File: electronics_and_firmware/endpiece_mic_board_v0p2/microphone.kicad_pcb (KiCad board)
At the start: 2 copper layers, 5.5 x 6 mm, 7 parts, among them J1 I2S_MIC_EXT, U1 SPH0645LMH

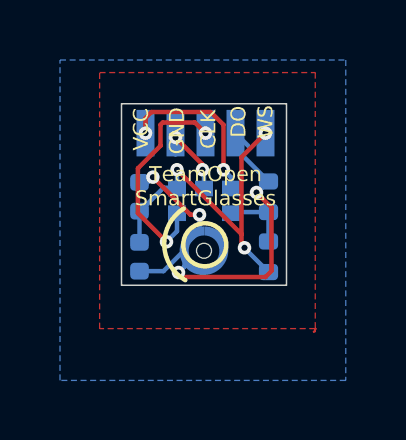
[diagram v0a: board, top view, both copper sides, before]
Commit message: change display MOSFET switch to p-type and switch high, thicken some traces on ext. i2s board, slide button down (check this fits capabilities), get rid of via in pad, move i2s line so not over top of psram lines
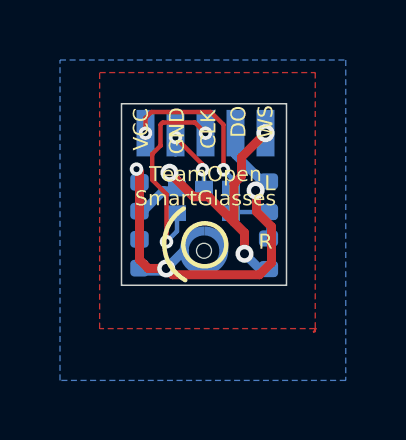
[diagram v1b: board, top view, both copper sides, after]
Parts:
- R1, R2: value 10K* -> 0R*
- moved C2 0.10 mm to (148.7, 96.4)
- moved R1 0.10 mm to (153.0, 96.4)
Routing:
- net GND: track 15.9 -> 16.3 mm, vias 4 -> 3
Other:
- board text added: "L"
- board text added: "R"
